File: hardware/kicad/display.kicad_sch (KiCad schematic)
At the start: 19 parts, among them J4 FPC-05FB-24PH20, Q7 SI1308EDL

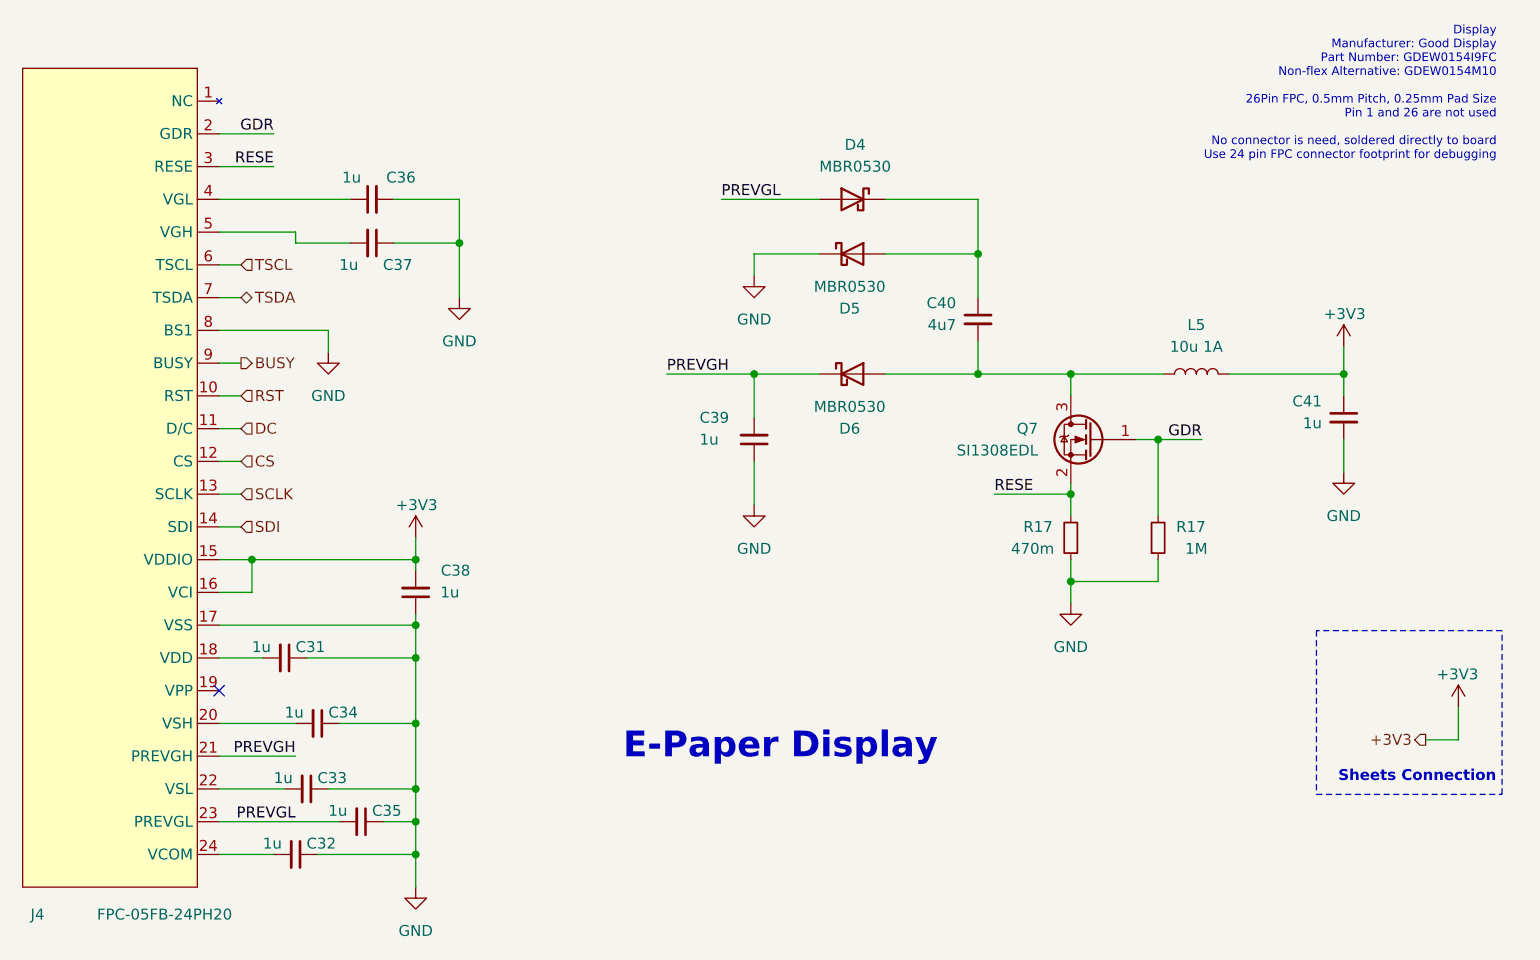
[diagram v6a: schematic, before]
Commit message: display sch done
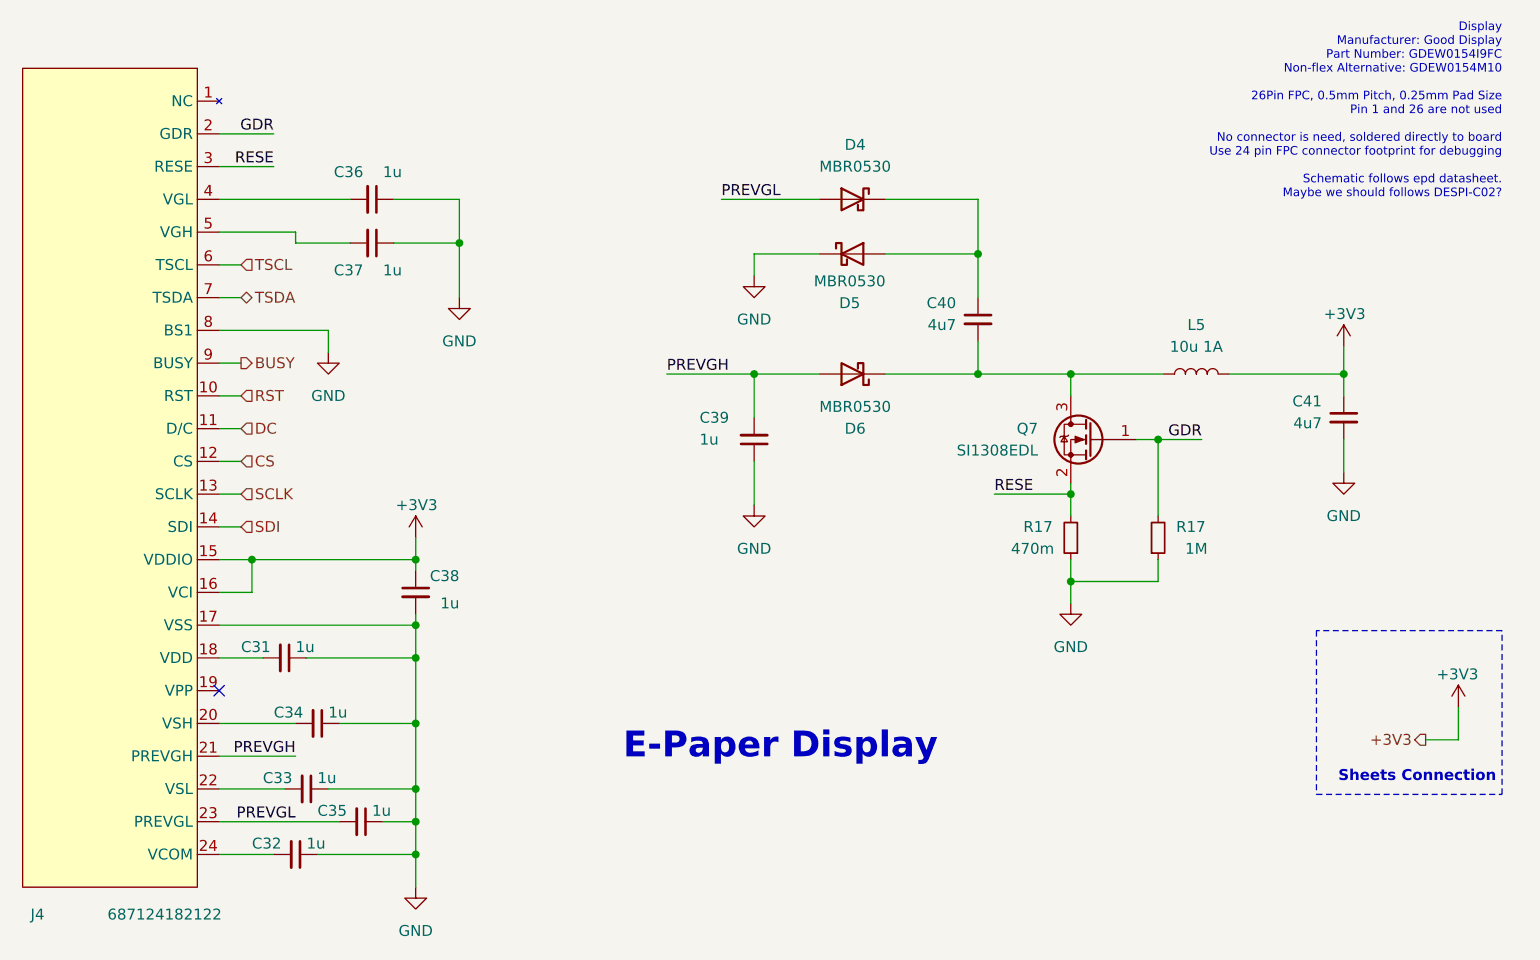
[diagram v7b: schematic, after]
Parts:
- C31, C32, C33, C34, C35, C36, C37, C38, C39: footprint (none) -> Capacitor_SMD:C_0402_1005Metric; Distributor (none) -> LCSC; Distributor Link (none) -> https://www.lcsc.com/product-detail/Multilayer-Ceramic-Capa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; Distributor Part Number (none) -> C1518208; Manufacturer (none) -> Murata Electronics; Manufacturer Part Number (none) -> GRM155R61H105KE05D; Part Description (none) -> Ceramic Capacitors 50V 1uF X5R ±10%
- C40: footprint (none) -> Capacitor_SMD:C_0603_1608Metric; Distributor (none) -> LCSC; Distributor Link (none) -> https://www.lcsc.com/product-detail/Multilayer-Ceramic-Capa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; Distributor Part Number (none) -> C69335; Manufacturer (none) -> Samsung Electro-Mechanics; Manufacturer Part Number (none) -> CL10A475KA8NQNC; Part Description (none) -> Ceramic Capacitors 25V 4.7uF X5R ±10%
- C41: value 1u -> 4u7; footprint (none) -> Capacitor_SMD:C_0603_1608Metric; Distributor (none) -> LCSC; Distributor Link (none) -> https://www.lcsc.com/product-detail/Multilayer-Ceramic-Capa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; Distributor Part Number (none) -> C69335; Manufacturer (none) -> Samsung Electro-Mechanics; Manufacturer Part Number (none) -> CL10A475KA8NQNC; Part Description (none) -> Ceramic Capacitors 25V 4.7uF X5R ±10%
- D4, D5, D6: Distributor (none) -> LCSC; Distributor Link (none) -> https://www.lcsc.com/product-detail/Schottky-Barrier-Diodes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; Distributor Part Number (none) -> C82046; Manufacturer (none) -> onsemi; Manufacturer Part Number (none) -> MBR0530T1G; Part Description (none) -> Schottky Barrier Diodes 30V 430mV@500mA 500mA
- J4: value FPC-05FB-24PH20 -> 687124182122; footprint (none) -> plantpal:687124182122; Distributor (none) -> Mouser; Distributor Link (none) -> https://www.mouser.com/ProductDetail/Wurth-Elektronik/68712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; Distributor Part Number (none) -> 710-687124182122; Manufacturer XUNPU -> Wurth Elektronik; Manufacturer Part Number (none) -> 687124182122; Part Description (none) -> FFC & FPC Connectors WR-FPC SMT Horiz 0.50mm Dual.Cont.; Part Number FPC-05FB-24PH20 -> (none)
- Q7: footprint Package_TO_SOT_SMD:SOT-23 -> Package_TO_SOT_SMD:SOT-323_SC-70; Distributor (none) -> LCSC; Distributor Link (none) -> https://www.lcsc.com/product-detail/MOSFETs_Vishay-Intertec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; Distributor Part Number (none) -> C469327; Manufacturer (none) -> Vishay Intertech; Manufacturer Part Number (none) -> SI1308EDL-T1-GE3; Part Description (none) -> MOSFET N Channel 30V 1.4A 132mΩ@10V,1.4A
- R17: Distributor (none) -> LCSC; Distributor Link (none) -> https://www.lcsc.com/product-detail/Chip-Resistor-Surface-M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; Distributor Part Number (none) -> C962578; Manufacturer (none) -> Vishay Intertech; Manufacturer Part Number (none) -> RCWE0402R470FKEA; Part Description Resistor 5.1K 1% 62.5mW -> Resistor 125mW ±1% 470mΩ
- R17: Distributor (none) -> LCSC; Distributor Link (none) -> https://www.lcsc.com/product-detail/Chip-Resistor-Surface-M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; Distributor Part Number (none) -> C159943; Manufacturer (none) -> KOA Speer Elec; Manufacturer Part Number (none) -> RK73H1ETTP1004F; Part Description Resistor 5.1K 1% 62.5mW -> Resistors 100mW ±1% 1MΩ
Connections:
- net +3V3: now also C38.1; no longer C38.2
- net GND: now also C36.1, C38.2; no longer C36.2, C38.1
- net PREVGH: now also D6.2 (A); no longer D6.1 (K)
- net at C40.2, L5.2, Q7.3 (D): now also D6.1 (K); no longer D6.2 (A)
- net at J4.4 (VGL): now also C36.2; no longer C36.1
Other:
- note added: "Display Manufacturer: Good Display Part Number: GDEW0154I9FC Non-flex Alternative: GDEW0154M10 26Pin FPC, 0.5mm Pitch, 0.25mm Pad Size Pin 1 and 26 are not used No connector is need, soldered directly to board Use 24 pin FPC connector footprint for debugging Schematic follows epd datasheet. Maybe we should follows DESPI-C02?"
- note removed: "Display Manufacturer: Good Display Part Number: GDEW0154I9FC Non-flex Alternative: GDEW0154M10 26Pin FPC, 0.5mm Pitch, 0.25mm Pad Size Pin 1 and 26 are not used No connector is need, soldered directly to board Use 24 pin FPC connector footprint for debugging"

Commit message: display sch done
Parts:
- L5: footprint (none) -> Inductor_SMD:L_Changjiang_FNR4012S; Distributor (none) -> LCSC; Distributor Link (none) -> https://www.lcsc.com/product-detail/Power-Inductors_cjiang-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; Distributor Part Number (none) -> C167785; Manufacturer (none) -> cjiang (Changjiang Microelectronics Tech); Manufacturer Part Number (none) -> FNR4012S100MT; Part Description (none) -> Power Inductors 1A 10uH ±20% 1.1A SMD,4x4mm
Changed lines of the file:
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@@
       (effects (font (size 1.27 1.27)))
     )
-    (property "Footprint" "" (at 160.655 53.975 0)
+    (property "Footprint" "Inductor_SMD:L_Changjiang_FNR4012S" (at 160.655 53.975 0)
       (effects (font (size 1.27 1.27)) hide)
     )
-    (property "Datasheet" "~" (at 160.655 53.975 0)
+    (property "Datasheet" "https://datasheet.lcsc.com/lcsc/2304140030_cjiang--Changjiang-Microelectronics-Tech-FNR4012S100MT_C167785.pdf" (at 160.655 53.975 0)
       (effects (font (size 1.27 1.27)) hide)
     )
+    (property "Part Description" "Power Inductors 1A 10uH ±20% 1.1A SMD,4x4mm " (at 160.655 53.975 0)
+      (effects (font (size 1.27 1.27)) hide)
+    )
+    (property "Manufacturer" "cjiang (Changjiang Microelectronics Tech)" (at 160.655 53.975 0)
+      (effects (font (size 1.27 1.27)) hide)
+    )
+    (property "Manufacturer Part Number" "FNR4012S100MT" (at 160.655 53.975 0)
+      (effects (font (size 1.27 1.27)) hide)
+    )
+    (property "Distributor" "LCSC" (at 160.655 53.975 0)
+      (effects (font (size 1.27 1.27)) hide)
+    )
+    (property "Distributor Part Number" "C167785" (at 160.655 53.975 0)
+      (effects (font (size 1.27 1.27)) hide)
+    )
+    (property "Distributor Link" "https://www.lcsc.com/product-detail/Power-Inductors_cjiang-Changjiang-Microelectronics-Tech-FNR4012S100MT_C167785.html" (at 160.655 53.975 0)
+      (effects (font (size 1.27 1.27)) hide)
+    )
